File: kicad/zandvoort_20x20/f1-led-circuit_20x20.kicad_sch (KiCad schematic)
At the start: 38 parts, among them J1 USB_C_Receptacle_USB2.0_14P, J2 Conn_ARM_JTAG_SWD_10_F1, Q1 TSM085P03CV_RGG, SW1 SW_SPST, SW2 SW_SPST, SW3 SW_SPDT, U1 HD108-2020, U2 HD108-2020, U200 ESP32-C3-MINI-1, U201 MCP9701AT-E/LT, U202 LDLN050, U203 NUF2042XV6T1G, U3 HD108-2020, U4 HD108-2020, U5 HD108-2020, U6 HD108-2020

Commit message: Add additional LEDs through hierarchical sheets
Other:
- added sheet LED_CHAIN10 (rgb_led_track_chain.kicad_sch)
- added sheet LED_CHAIN11 (rgb_led_track_chain.kicad_sch)
- added sheet LED_CHAIN12 (rgb_led_track_chain.kicad_sch)
- added sheet LED_CHAIN5 (rgb_led_track_chain.kicad_sch)
- added sheet LED_CHAIN6 (rgb_led_track_chain.kicad_sch)
- added sheet LED_CHAIN7 (rgb_led_track_chain.kicad_sch)
- added sheet LED_CHAIN8 (rgb_led_track_chain.kicad_sch)
- added sheet LED_CHAIN9 (rgb_led_track_chain.kicad_sch)
- moved on the sheet: C9, J2, JP1, NT1, NT2, R6, R7, R8, U200

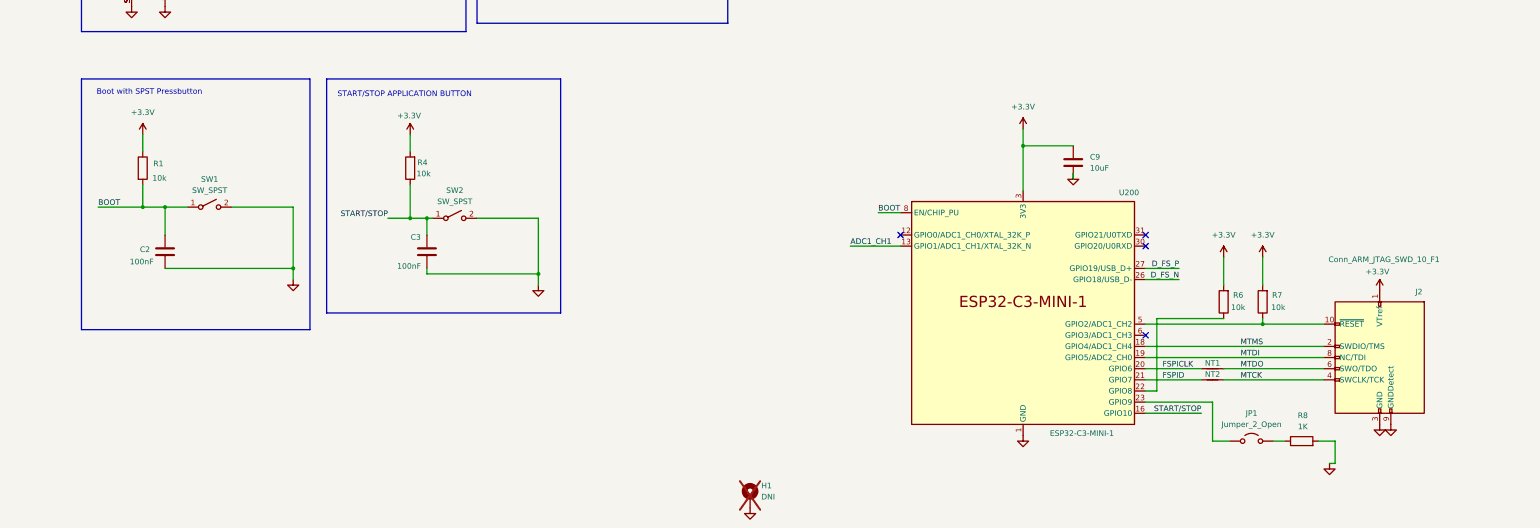
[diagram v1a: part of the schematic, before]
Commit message: Add test points for jumper and JTAG
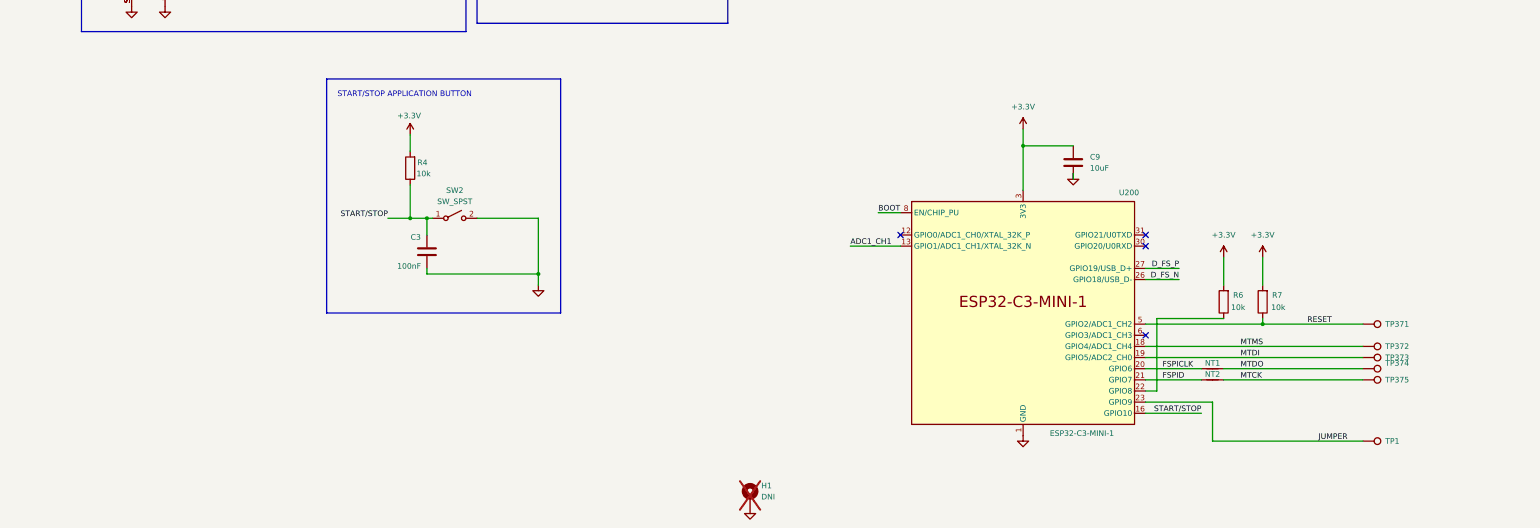
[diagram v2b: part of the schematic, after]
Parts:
- removed C2: 100nF, Capacitor_SMD:C_0402_1005Metric, symbol Device:C
- removed J2: Conn_ARM_JTAG_SWD_10_F1, F1-LED-CIRCUIT-LIBRARY:SAMTEC_FTSH-105-XX-X-DV, symbol F1-LED-CIRCUIT-LIBRARY:Conn_ARM_JTAG_SWD_10_F1
- removed JP1: Jumper_2_Open, Connector_PinHeader_2.54mm:PinHeader_1x02_P2.54mm_Vertical, symbol Jumper:Jumper_2_Open
- removed R1: 10k, Resistor_SMD:R_0402_1005Metric, symbol Device:R
- removed R8: 1K, Resistor_SMD:R_0402_1005Metric, symbol Device:R
- removed SW1: SW_SPST, F1-LED-CIRCUIT-LIBRARY:WS-TASV-SPST-6x6mm, symbol Switch:SW_SPST
- added TP1, TP371, TP372, TP373, TP374, TP375: TestPoint, symbol adams_library_symbols:TestPoint
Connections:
- net MTCK: now also TP375.1
- net MTDI: now also TP373.1
- net MTDO: now also TP374.1
- net MTMS: now also TP372.1
- net RESET: now reaches R7.1, U200.5 (GPIO2/ADC1_CH2)
- net RESET: now also TP371.1
- net JUMPER: now reaches U200.23 (GPIO9)
- net JUMPER: now also TP1.1
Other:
- note removed: "Boot with SPST Pressbutton"

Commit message: Add leds to schematic and place in layout
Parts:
- removed H1: DNI, MountingHole:MountingHole_4.3mm_M4_Pad_Via, symbol Mechanical:MountingHole_Pad_MP
- added U7, U8, U9: HD108-2020, F1-LED-CIRCUIT-LIBRARY:HD108-2020, symbol F1-LED-CIRCUIT-LIBRARY:HD108-2020
- TP1, TP371, TP372, TP373, TP374, TP375: footprint (none) -> TestPoint:TestPoint_Pad_D1.5mm
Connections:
- net +5V: now also U7.1 (VDD), U8.1 (VDD), U9.1 (VDD)
- net GND: now also U7.4 (GND), U8.4 (GND), U9.4 (GND)
- net LED_CHAIN1/DCKI: now also U9.2 (DCKO); no longer U6.2 (DCKO)
- net LED_CHAIN1/DIN: now also U9.3 (DOUT); no longer U6.3 (DOUT)
- new net: U8.2 (DCKO), U9.5 (DCKI)
- new net: U8.3 (DOUT), U9.6 (DIN)
- new net: U7.2 (DCKO), U8.5 (DCKI)
- new net: U7.3 (DOUT), U8.6 (DIN)
- new net: U6.2 (DCKO), U7.5 (DCKI)
- new net: U6.3 (DOUT), U7.6 (DIN)
- no-connect marks 7 -> 5
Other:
- removed sheet LED_CHAIN10
- removed sheet LED_CHAIN11
- removed sheet LED_CHAIN12
- removed sheet LED_CHAIN8
- removed sheet LED_CHAIN9
- moved on the sheet: C10, C8, U201

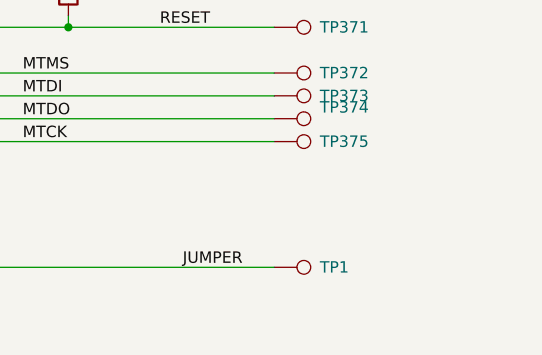
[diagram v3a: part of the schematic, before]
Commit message: Move power components to B.Cu and route
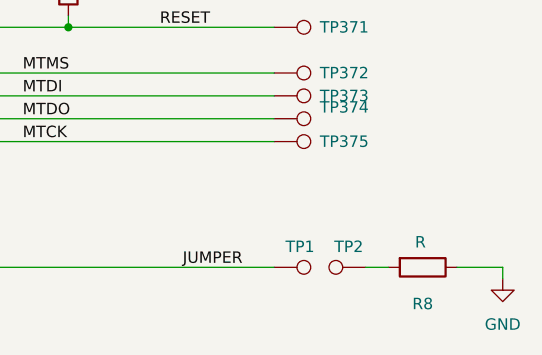
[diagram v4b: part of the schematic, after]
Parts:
- added R8: R, Resistor_SMD:R_0402_1005Metric, symbol Device:R
- added TP2: TestPoint, TestPoint:TestPoint_Pad_D1.5mm, symbol adams_library_symbols:TestPoint
- Q1: footprint JITTER-COMPONENTS:PDFN33-1EP_3x3mm_P0.65mm -> F1-LED-CIRCUIT-LIBRARY:PDFN33-1EP_3x3mm_P0.65mm
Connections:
- net GND: now also R8.1
- new net: R8.2, TP2.1
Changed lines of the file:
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@@
 	(wire
 		(pts
+			(xy 336.55 242.57) (xy 339.09 242.57)
+		)
+		(stroke
+			(width 0)
+			(type default)
+		)
+	)
+	(wire
+		(pts
 			(xy 134.62 109.22) (xy 134.62 111.76)
 		)
@@
 	(wire
 		(pts
+			(xy 346.71 242.57) (xy 351.79 242.57)
+		)
+		(stroke
+			(width 0)
+			(type default)
+		)
+	)
+	(wire
+		(pts
 			(xy 279.4 214.63) (xy 279.4 231.14)
 		)
@@
 	(wire
 		(pts
+			(xy 351.79 242.57) (xy 351.79 243.84)
+		)
+		(stroke
+			(width 0)
+			(type default)
+		)
+	)
+	(wire
+		(pts
 			(xy 228.6 52.07) (xy 232.41 52.07)
 		)
@@
 	(symbol
 		(lib_id "Device:R")
+		(at 342.9 242.57 270)
+		(unit 1)
+		(exclude_from_sim no)
+		(in_bom yes)
+		(on_board yes)
+		(dnp no)
+		(property "Reference" "R8"
+			(at 342.9 246.634 90)
+			(effects
+				(font
+					(size 1.27 1.27)
+				)
+			)
+		)
+		(property "Value" "R"
+			(at 342.646 239.776 90)
+			(effects
+				(font
+					(size 1.27 1.27)
+				)
+			)
+		)
+		(property "Footprint" "Resistor_SMD:R_0402_1005Metric"
+			(at 342.9 240.792 90)
+			(effects
+				(font
+					(size 1.27 1.27)
+				)
+				(hide yes)
+			)
+		)
+		(property "Datasheet" "~"
+			(at 342.9 242.57 0)
+			(effects
+				(font
+					(size 1.27 1.27)
+				)
+				(hide yes)
+			)
+		)
+		(property "Description" "Resistor"
+			(at 342.9 242.57 0)
+			(effects
+				(font
+					(size 1.27 1.27)
+				)
+				(hide yes)
+			)
+		)
+		(pin "2"
+		)
+		(pin "1"
+		)
+		(instances
+			(project "f1-led-circuit_20x20"
+				(path "/e1a94fd7-a746-413d-af87-306e7f792800"
+					(reference "R8")
+					(unit 1)
+				)
+			)
+		)
+	)
+	(symbol
+		(lib_id "Device:R")
 		(at 109.22 180.34 180)
 		(unit 1)
@@
 		(on_board yes)
 		(dnp no)
-		(fields_autoplaced yes)
 		(property "Reference" "TP1"
-			(at 331.47 242.5699 90)
+			(at 327.66 240.284 90)
 			(effects
 				(font
@@
 			)
 		)
-		(property "Footprint" "JITTER-COMPONENTS:PDFN33-1EP_3x3mm_P0.65mm"
+		(property "Footprint" "F1-LED-CIRCUIT-LIBRARY:PDFN33-1EP_3x3mm_P0.65mm"
 			(at 142.875 106.68 0)
 			(effects
@@
 	)
 	(symbol
+		(lib_id "adams_library_symbols:TestPoint")
+		(at 336.55 242.57 90)
+		(unit 1)
+		(exclude_from_sim no)
+		(in_bom yes)
+		(on_board yes)
+		(dnp no)
+		(property "Reference" "TP2"
+			(at 336.296 240.284 90)
+			(effects
+				(font
+					(size 1.27 1.27)
+				)
+				(justify left)
+			)
+		)
+		(property "Value" "TestPoint"
+			(at 331.47 241.3001 90)
+			(effects
+				(font
+					(size 1.27 1.27)
+				)
+				(justify left)
+				(hide yes)
+			)
+		)
+		(property "Footprint" "TestPoint:TestPoint_Pad_D1.5mm"
+			(at 336.55 237.49 0)
+			(effects
+				(font
+					(size 1.27 1.27)
+				)
+				(hide yes)
+			)
+		)
+		(property "Datasheet" "~"
+			(at 336.55 237.49 0)
+			(effects
+				(font
+					(size 1.27 1.27)
+				)
+				(hide yes)
+			)
+		)
+		(property "Description" "test point"
+			(at 336.55 242.57 0)
+			(effects
+				(font
+					(size 1.27 1.27)
+				)
+				(hide yes)
+			)
+		)
+		(pin "1"
+		)
+		(instances
+			(project "f1-led-circuit_20x20"
+				(path "/e1a94fd7-a746-413d-af87-306e7f792800"
+					(reference "TP2")
+					(unit 1)
+				)
+			)
+		)
+	)
+	(symbol
 		(lib_id "Device:R")
 		(at 76.2 113.03 270)
@@
 					(unit 1)
 				)
+			)
+		)
+	)
+	(symbol
+		(lib_id "power:GND")
+		(at 351.79 243.84 0)
+		(unit 1)
+		(exclude_from_sim no)
+		(in_bom yes)
+		(on_board yes)
+		(dnp no)
+		(fields_autoplaced yes)
+		(property "Reference" "#PWR0302"
+			(at 351.79 250.19 0)
+			(effects
+				(font
+					(size 1.27 1.27)
+				)
+				(hide yes)
+			)
+		)
+		(property "Value" "GND"
+			(at 351.79 248.92 0)
+			(effects
+				(font
+					(size 1.27 1.27)
+				)
+			)
+		)
+		(property "Footprint" ""
+			(at 351.79 243.84 0)
+			(effects
+				(font
+					(size 1.27 1.27)
+				)
+				(hide yes)
+			)
+		)
+		(property "Datasheet" ""
+			(at 351.79 243.84 0)
+			(effects
+				(font
+					(size 1.27 1.27)
+				)
+				(hide yes)
+			)
+		)
+		(property "Description" "Power symbol creates a global label with name \"GND\" , ground"
+			(at 351.79 243.84 0)
+			(effects
+				(font
+					(size 1.27 1.27)
+				)
+				(hide yes)
+			)
+		)
+		(pin "1"
+		)
+		(instances
+			(project "f1-led-circuit_20x20"
+				(path "/e1a94fd7-a746-413d-af87-306e7f792800"
+					(reference "#PWR0302")
+					(unit 1)
+				)

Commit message: Update part number for MCU
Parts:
- U200: MPN ESP32-C3-MINI-1U-N4 -> ESP32-C3-MINI-1-N4
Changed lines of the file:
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@@
 			)
 		)
-		(property "MPN" "ESP32-C3-MINI-1U-N4"
+		(property "MPN" "ESP32-C3-MINI-1-N4"
 			(at 248.92 213.36 0)
 			(effects

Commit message: KiCad - Update designator numbers for LEDS
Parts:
- removed U7, U8, U9: HD108-2020, F1-LED-CIRCUIT-LIBRARY:HD108-2020, symbol F1-LED-CIRCUIT-LIBRARY:HD108-2020
- renumbered U200 to U300, U201 to U301, U202 to U302, U203 to U303
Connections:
- net LED_CHAIN1/DCKI: now also U6.2 (DCKO)
- net LED_CHAIN1/DIN: now also U6.3 (DOUT)
- no-connect marks 5 -> 7

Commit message: Add Boot with Test Points
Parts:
- added C?: 100nF, Capacitor_SMD:C_0402_1005Metric, symbol Device:C
- added R?: 10k, Resistor_SMD:R_0402_1005Metric, symbol Device:R
- added TP1, TP2: TestPoint, symbol Connector:TestPoint
- renumbered TP375 to TP10, TP371 to TP3, TP1 to TP5, TP2 to TP6, TP372 to TP7, TP373 to TP8, TP374 to TP9
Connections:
- net +3.3V: now also R?.1
- net BOOT: now also C?.2, R?.2, TP1.1
- net GND: now also C?.1, TP2.1
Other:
- note added: "BOOT WITH TEST POINTS"
- moved on the sheet: C3, R4, SW2

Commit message: Update test points - Add 3D models - Update SON_2XV6T1G_ONS.kicad_mod footprint
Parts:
- gave numbers to parts that had none: 2
- renumbered TP7 to TP4, TP8 to TP5, TP9 to TP6, TP10 to TP7, TP5 to TP8, TP6 to TP9
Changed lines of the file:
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@@
 		(on_board yes)
 		(dnp no)
-		(property "Reference" "R?"
+		(property "Reference" "R1001"
 			(at 51.816 176.784 0)
 			(effects
@@
 			(project "f1-led-circuit_20x20"
 				(path "/e1a94fd7-a746-413d-af87-306e7f792800"
-					(reference "R?")
+					(reference "R1001")
 					(unit 1)
 				)
@@
 		(dnp no)
 		(fields_autoplaced yes)
-		(property "Reference" "TP9"
+		(property "Reference" "TP6"
 			(at 331.47 226.0599 90)
 			(effects
@@
 			(project "f1-led-circuit_20x20"
 				(path "/e1a94fd7-a746-413d-af87-306e7f792800"
-					(reference "TP9")
+					(reference "TP6")
 					(unit 1)
 				)
@@
 		(dnp no)
 		(fields_autoplaced yes)
-		(property "Reference" "TP10"
+		(property "Reference" "TP7"
 			(at 331.47 228.5999 90)
 			(effects
@@
 			(project "f1-led-circuit_20x20"
 				(path "/e1a94fd7-a746-413d-af87-306e7f792800"
-					(reference "TP10")
+					(reference "TP7")
 					(unit 1)
 				)
@@
 		(on_board yes)
 		(dnp no)
-		(property "Reference" "C?"
+		(property "Reference" "C1001"
 			(at 48.768 196.342 0)
 			(effects
@@
 			(project "f1-led-circuit_20x20"
 				(path "/e1a94fd7-a746-413d-af87-306e7f792800"
-					(reference "C?")
+					(reference "C1001")
 					(unit 1)
 				)
@@
 		(on_board yes)
 		(dnp no)
-		(property "Reference" "TP5"
+		(property "Reference" "TP8"
 			(at 327.66 240.284 90)
 			(effects
@@
 			(project "f1-led-circuit_20x20"
 				(path "/e1a94fd7-a746-413d-af87-306e7f792800"
-					(reference "TP5")
+					(reference "TP8")
 					(unit 1)
 				)
@@
 		(on_board yes)
 		(dnp no)
-		(property "Reference" "TP6"
+		(property "Reference" "TP9"
 			(at 336.296 240.284 90)
 			(effects
@@
 			(project "f1-led-circuit_20x20"
 				(path "/e1a94fd7-a746-413d-af87-306e7f792800"
-					(reference "TP6")
+					(reference "TP9")
 					(unit 1)
 				)
@@
 		(dnp no)
 		(fields_autoplaced yes)
-		(property "Reference" "TP7"
+		(property "Reference" "TP4"
 			(at 331.47 220.9799 90)
 			(effects
@@
 			(project "f1-led-circuit_20x20"
 				(path "/e1a94fd7-a746-413d-af87-306e7f792800"
-					(reference "TP7")
+					(reference "TP4")
 					(unit 1)
 				)
@@
 		(dnp no)
 		(fields_autoplaced yes)
-		(property "Reference" "TP8"
+		(property "Reference" "TP5"
 			(at 331.47 223.5199 90)
 			(effects
@@
 			(project "f1-led-circuit_20x20"
 				(path "/e1a94fd7-a746-413d-af87-306e7f792800"
-					(reference "TP8")
+					(reference "TP5")
 					(unit 1)
 				)
